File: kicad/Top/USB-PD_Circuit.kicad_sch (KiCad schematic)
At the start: 57 parts

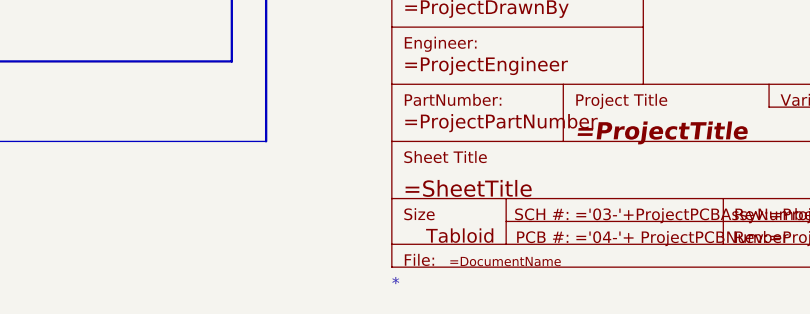
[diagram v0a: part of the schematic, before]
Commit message: Properly synced pcb to schematic
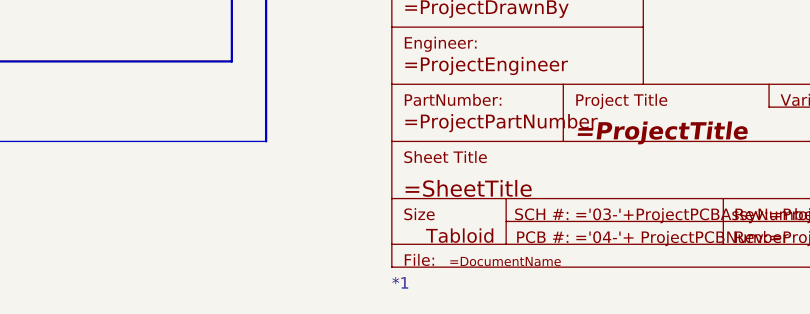
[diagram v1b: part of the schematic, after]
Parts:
- C18, C46: value ~ -> Capacitor NP; footprint (none) -> AltiumImports:_ALTIUM_WORK_00001_MCHP-CDB_Library_Database_MCHP-CDB.DbLib_Capacitor_CAP_C_0603
- C19, C20: value ~ -> Capacitor NP; footprint (none) -> AltiumImports:_ALTIUM_WORK_00001_MCHP-CDB_Library_Database_.._Footprints_CAP_C_0603.PcbLib_CAP_C_0603
- C25, C32, C47, C48: value ~ -> Capacitor NP; footprint (none) -> AltiumImports:_ALTIUM_WORK_00001_MCHP-CDB_Library_Database_MCHP-CDB.DbLib_Capacitor_CAP_C_0402
- C33, C44, C45: value ~ -> CAP1337; footprint (none) -> AltiumImports:_ALTIUM_WORK_00001_MCHP-CDB_Library_Database_.._Footprints_CAP_C_0402.PcbLib_CAP_C_0402
- C49, C51, C52: value ~ -> CAP1337; footprint (none) -> AltiumImports:CAP_C_0402
- C50: value ~ -> Capacitor NP; footprint (none) -> AltiumImports:CAP_C_0603
- D15, D17: value ~ -> LED_green; footprint (none) -> AltiumImports:_ALTIUM_WORK_00001_MCHP-CDB_Library_Database_.._Footprints_LED_0603_Green.PcbLib_LED_0603_GREEN
- D16: value ~ -> Diode Dual AK; footprint (none) -> AltiumImports:SOT-23-3
- D18: value ~ -> LED_orange; footprint (none) -> AltiumImports:_ALTIUM_WORK_00001_MCHP-CDB_Library_Database_.._Footprints_LED_0603_Orange.PcbLib_LED_0603_Orange
- FB1: value ~ -> Ferrite Bead; footprint (none) -> AltiumImports:IND_C_0603
- J4: value ~ -> USBC_Receptacle_SMD_RA; footprint (none) -> AltiumImports:CON_USB3.1-C_RCPT_SMD_RA_ACP_12401610E4#2A
- Q6, Q7: value ~ -> SI4477DY-T1-GE3; footprint (none) -> AltiumImports:_ALTIUM_WORK_00001_MCHP-CDB_Library_Database_.._Footprints_SOIC-8.PcbLib_SOIC-8
- Q8, Q9: value ~ -> PMBF170,235; footprint (none) -> AltiumImports:NXP-SOT23_M
- R11: value ~ -> Resistor; footprint (none) -> AltiumImports:RES_C_1206
- R23, R24, R27, R33, R50, R52: value ~ -> Resistor; footprint (none) -> AltiumImports:_ALTIUM_WORK_00001_MCHP-CDB_Library_Database_MCHP-CDB.DbLib_Resistor_RES_C_0402
- R28, R34, R35, R48, R54, R55: value ~ -> CRGP0402F10K; footprint (none) -> AltiumImports:FP-CRGP0402-IPC_A
- R31, R49: value ~ -> Resistor; footprint (none) -> AltiumImports:_ALTIUM_WORK_00001_MCHP-CDB_Library_Database_MCHP-CDB-Offline.DbLib_Resistor_RES_C_0402
- R32, R47, R51, R53: value ~ -> Resistor; footprint (none) -> AltiumImports:_ALTIUM_WORK_00001_MCHP-CDB_Library_Database_.._Footprints_RES_C_0402.PcbLib_RES_C_0402
- R36: value ~ -> CMP-2002-07613-1; footprint (none) -> AltiumImports:RESC1005X40X25LL05T10
- TP13, TP14, TP52, TP53, TP54, TP55, TP56, TP57, TP58: value ~ -> Test Point No BOM; footprint (none) -> AltiumImports:_ALTIUM_WORK_00001_MCHP-CDB_Library_Database_.._Footprints_TP_1mm_SMD.PcbLib_TP_1mm_SMD
- U3: value ~ -> MCP1804 SOT-23-5; footprint (none) -> AltiumImports:_ALTIUM_WORK_00001_MCHP-CDB_Library_Database_MCHP-CDB.DbLib_MCHP-Analog_SOT-23-5
- U4: value ~ -> UPD301C QFN-40; footprint QFN-40_6X6_m5_4m6epad -> AltiumImports:_ALTIUM_WORK_00001_MCHP-CDB_Library_Database_MCHP-CDB.DbLib_MCHP-Interface_QFN-40_6X6_m5_4m6epad
- renumbered * to *1

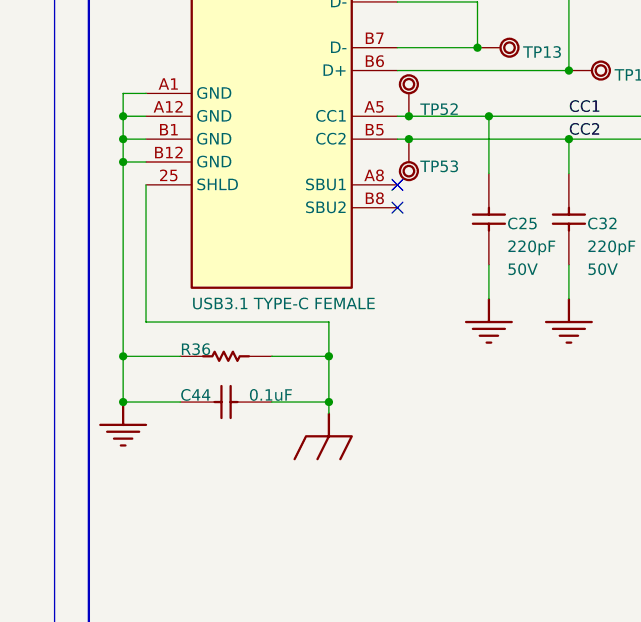
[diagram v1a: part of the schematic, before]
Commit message: Removed earth net
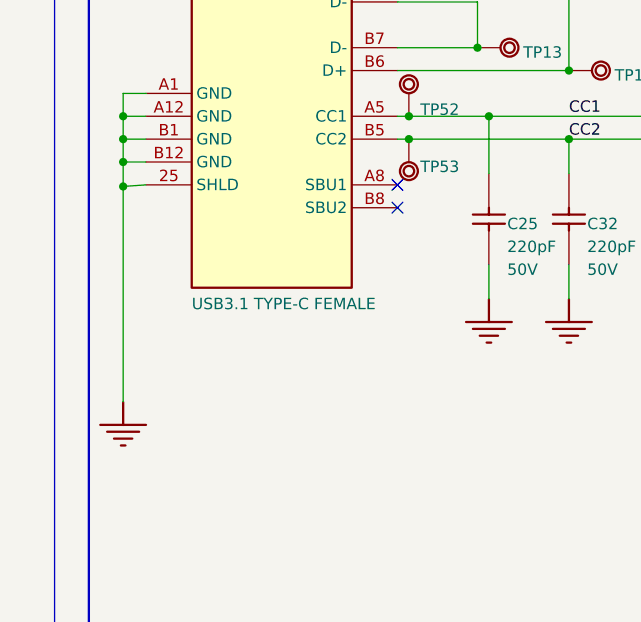
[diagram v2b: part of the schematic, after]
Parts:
- removed C44: CAP1337, AltiumImports:_ALTIUM_WORK_00001_MCHP-CDB_Library_Database_.._Footprints_CAP_C_0402.PcbLib_CAP_C_0402, symbol Top-altium-import:2_CAP1337
- removed R36: CMP-2002-07613-1, AltiumImports:RESC1005X40X25LL05T10, symbol Top-altium-import:0_RES
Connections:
- net EARTH_P1 is gone; now on net PGND: J4.25 (SHLD)

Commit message: WIP, adding 3-pin pad symbol for smd R0 selection
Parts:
- removed *1: ~, symbol Top-altium-import:0_Title Block Tabloid
- removed C19, C20: Capacitor NP, AltiumImports:_ALTIUM_WORK_00001_MCHP-CDB_Library_Database_.._Footprints_CAP_C_0603.PcbLib_CAP_C_0603, symbol Top-altium-import:1_Capacitor NP
- removed C33, C45: CAP1337, AltiumImports:_ALTIUM_WORK_00001_MCHP-CDB_Library_Database_.._Footprints_CAP_C_0402.PcbLib_CAP_C_0402, symbol Top-altium-import:1_CAP1337
- removed C46: Capacitor NP, AltiumImports:_ALTIUM_WORK_00001_MCHP-CDB_Library_Database_MCHP-CDB.DbLib_Capacitor_CAP_C_0603, symbol Top-altium-import:1_Capacitor NP
- removed C47, C48: Capacitor NP, AltiumImports:_ALTIUM_WORK_00001_MCHP-CDB_Library_Database_MCHP-CDB.DbLib_Capacitor_CAP_C_0402, symbol Top-altium-import:1_Capacitor NP
- removed C49, C51, C52: CAP1337, AltiumImports:CAP_C_0402, symbol Top-altium-import:3_CAP1337
- removed C50: Capacitor NP, AltiumImports:CAP_C_0603, symbol Top-altium-import:1_Capacitor NP
- removed D15: LED_green, AltiumImports:_ALTIUM_WORK_00001_MCHP-CDB_Library_Database_.._Footprints_LED_0603_Green.PcbLib_LED_0603_GREEN, symbol Top-altium-import:3_LED_green
- removed D16: Diode Dual AK, AltiumImports:SOT-23-3, symbol Top-altium-import:2_mirrored_Diode Dual AK
- removed D17: LED_green, AltiumImports:_ALTIUM_WORK_00001_MCHP-CDB_Library_Database_.._Footprints_LED_0603_Green.PcbLib_LED_0603_GREEN, symbol Top-altium-import:0_LED_green
- removed D18: LED_orange, AltiumImports:_ALTIUM_WORK_00001_MCHP-CDB_Library_Database_.._Footprints_LED_0603_Orange.PcbLib_LED_0603_Orange, symbol Top-altium-import:0_LED_orange
- removed FB1: Ferrite Bead, AltiumImports:IND_C_0603, symbol Top-altium-import:0_Ferrite Bead
- removed Q8: PMBF170,235, AltiumImports:NXP-SOT23_M, symbol Top-altium-import:0_mirrored_CMP-1258-00138-1
- removed Q9: PMBF170,235, AltiumImports:NXP-SOT23_M, symbol Top-altium-import:0_CMP-1258-00138-1
- removed R11: Resistor, AltiumImports:RES_C_1206, symbol Top-altium-import:1_Resistor
- removed R23, R24: Resistor, AltiumImports:_ALTIUM_WORK_00001_MCHP-CDB_Library_Database_MCHP-CDB.DbLib_Resistor_RES_C_0402, symbol Top-altium-import:3_Resistor
- removed R27: Resistor, AltiumImports:_ALTIUM_WORK_00001_MCHP-CDB_Library_Database_MCHP-CDB.DbLib_Resistor_RES_C_0402, symbol Top-altium-import:2_Resistor
- removed R28: CRGP0402F10K, AltiumImports:FP-CRGP0402-IPC_A, symbol Top-altium-import:2_CMP-03211-008310-1
- removed R31: Resistor, AltiumImports:_ALTIUM_WORK_00001_MCHP-CDB_Library_Database_MCHP-CDB-Offline.DbLib_Resistor_RES_C_0402, symbol Top-altium-import:1_Resistor
- removed R33: Resistor, AltiumImports:_ALTIUM_WORK_00001_MCHP-CDB_Library_Database_MCHP-CDB.DbLib_Resistor_RES_C_0402, symbol Top-altium-import:1_Resistor
- removed R34, R35, R48, R54, R55: CRGP0402F10K, AltiumImports:FP-CRGP0402-IPC_A, symbol Top-altium-import:1_CMP-03211-008310-1
- removed R47: Resistor, AltiumImports:_ALTIUM_WORK_00001_MCHP-CDB_Library_Database_.._Footprints_RES_C_0402.PcbLib_RES_C_0402, symbol Top-altium-import:0_Resistor
- removed R49: Resistor, AltiumImports:_ALTIUM_WORK_00001_MCHP-CDB_Library_Database_MCHP-CDB-Offline.DbLib_Resistor_RES_C_0402, symbol Top-altium-import:0_Resistor
- removed R50, R52: Resistor, AltiumImports:_ALTIUM_WORK_00001_MCHP-CDB_Library_Database_MCHP-CDB.DbLib_Resistor_RES_C_0402, symbol Top-altium-import:0_Resistor
- removed R53: Resistor, AltiumImports:_ALTIUM_WORK_00001_MCHP-CDB_Library_Database_.._Footprints_RES_C_0402.PcbLib_RES_C_0402, symbol Top-altium-import:2_Resistor
- removed TP54, TP55, TP56, TP57, TP58: Test Point No BOM, AltiumImports:_ALTIUM_WORK_00001_MCHP-CDB_Library_Database_.._Footprints_TP_1mm_SMD.PcbLib_TP_1mm_SMD, symbol Top-altium-import:0_Test Point No BOM
- removed U3: MCP1804 SOT-23-5, AltiumImports:_ALTIUM_WORK_00001_MCHP-CDB_Library_Database_MCHP-CDB.DbLib_MCHP-Analog_SOT-23-5, symbol Top-altium-import:0_MCP1804 SOT-23-5
- removed U4: UPD301C QFN-40, AltiumImports:_ALTIUM_WORK_00001_MCHP-CDB_Library_Database_MCHP-CDB.DbLib_MCHP-Interface_QFN-40_6X6_m5_4m6epad, symbol Top-altium-import:0_UPD301C QFN-40
- added C?: 100nF, symbol Device:C_Small
- added C? (x3): 1uF, symbol Device:C_Small
- added D? (x2): ESDA25P35-1U1M, custom_modules:ESDA25P35-1U1M, symbol ESDA25P35-1U1M:ESDA25P35-1U1M
- added D?: ESDA25W, custom_modules:ESDA25W, symbol ESDA25W:ESDA25W
- added R? (x2): 100k, symbol Device:R_Small_US
- added R? (x2): R_Small_US, symbol Device:R_Small_US
- added R?: 100, symbol Device:R_Small_US
- added R?: 22k, symbol Device:R_Small_US
- added R?: 10K, symbol Device:R_Small_US
- added R?: 1k, symbol Device:R_Small_US
- added U?: STUSB4500BJR, custom_modules:STUSB4500BJR, symbol STUSB4500BJR:STUSB4500BJR
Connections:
- net VBUS_USB is gone; now on net VSNK: Q6.5 (D), Q6.6 (D), Q6.7 (D), Q6.8 (D)
- net AGND: now also C?.1, C?.1, C?.1, D?.3, R?.1, R?.2, R?.2, U?.B1 (VSYS), U?.B3 (NC), U?.C3 (NC), U?.E3 (GND)
- net CC1: now also D?.2, U?.B4 (CC1DB), U?.B5 (CC1)
- net CC2: now also D?.1, U?.C4 (CC2DB), U?.C5 (CC2)
- net PGND: now also D?.2, D?.2; no longer R32.1
- net VBUS_F: now also R32.2, C?.2, U?.A5 (VDD)
- net at Q6.4 (G), Q7.4 (G): now also R32.1, R?.1, R?.2
- net VSNK: now reaches R51.2
- net VSNK: now also C?.1, D?.1
- net at C18.2, J4.A4 (VBUS), J4.A9 (VBUS)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: now also D?.1, R?.1
- net EN_SNK: no longer names the net of R51.1
- net EN_SNK: now also U?.E4 (DISCH); no longer R32.2
- new net: R?.1, R?.1, U?.D3 (ADDR0)
- new net: C?.2, R?.2
- new net: C?.2, U?.A3 (VREG__1V2)
- new net: R?.2, U?.A1 (VBUS_VS__DISCH)
- new net: R?.1, U?.C1 (VBUS__EN_SNK)
- new net: R?.1, R?.1, U?.D2 (ADDR1)
- new net 2V7: C?.2, R?.2, R?.2, U?.A4 (VREG__2V7)
- new net STUSB_ALERT: U?.B2 (ALERT)
- new net STUSB_RESET: R?.2, U?.D4 (RESET)
- new net STUSB_SCL: U?.D5 (SCL)
- new net STUSB_SDA: U?.E5 (SDA)
- no-connect marks 27 -> 10
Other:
- note removed: ""3V3""
- note removed: ""CAP_MIS""
- note removed: ""EN_SNK""
- note removed: "10:1 VBUS_DET"
- note removed: "3V3 @ 150mA"
- note removed: "EVB-UPD301 Basic Sink Essential Circuitry"
- note removed: "HARNESS: USB_POWER"
- note removed: "Internal SAMD20 Bypass Caps"
- note removed: "Internal UPD350 Bypass Caps"
- note removed: "Place FB1 near VDDANA"
- note removed: "UPD301C"
- note removed: "VBUS (5-20VDC) to 3.3VDC"
- note removed: "VBUS Sink Load Switch/ Output Connector"
- moved on the sheet: C18, C25, C32, J4, Q6, Q7, R32, R51, TP13, TP14, TP52, TP53
